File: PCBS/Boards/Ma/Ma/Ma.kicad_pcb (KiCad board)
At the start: 2 copper layers, 25 x 25 mm, 15 parts, among them J1 Conn_01x20_Socket, J2 Programmer, J3 PWM CHANNELS, J4 OLED SCREEN, SW1 SW_SPST, U1 ATmega328P-M, Y1 16MHz

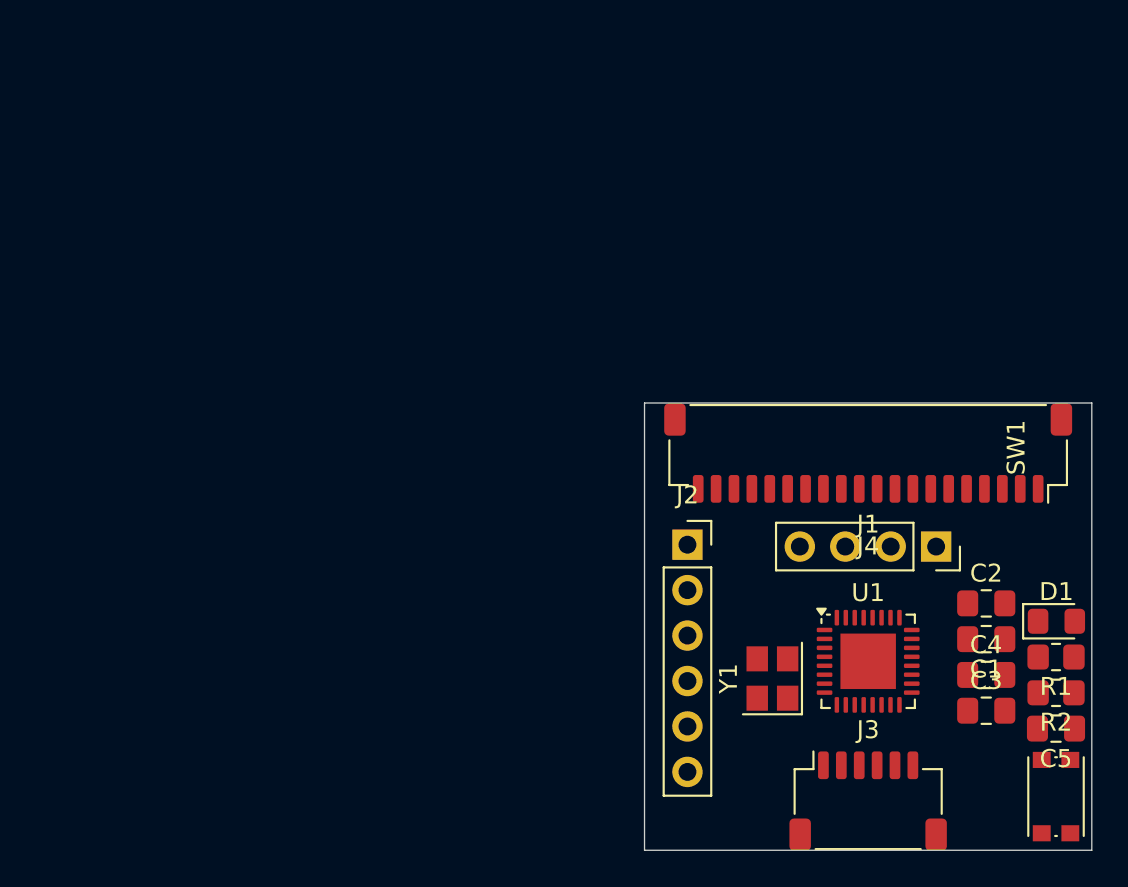
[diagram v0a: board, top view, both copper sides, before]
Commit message: creates schematic and PCB for MA minisumo board
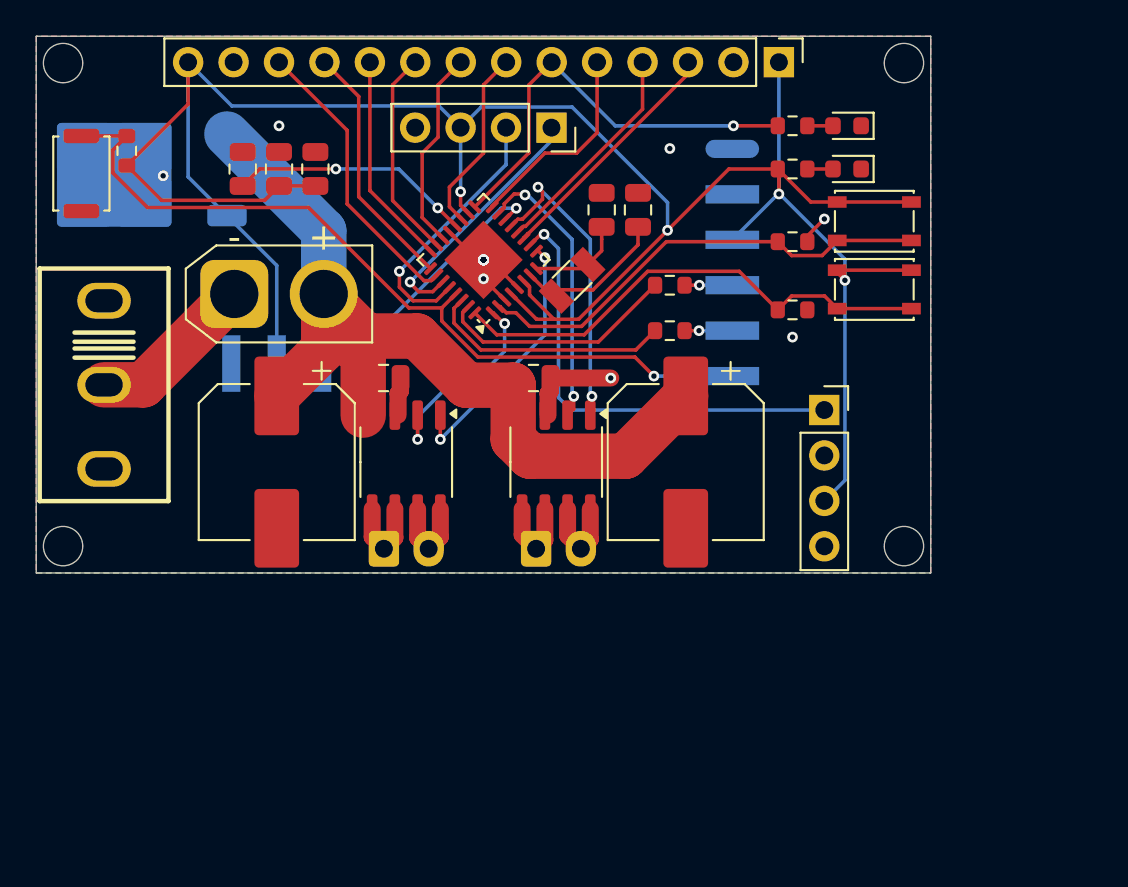
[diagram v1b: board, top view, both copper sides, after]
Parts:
- added C10: 0.1uF, Capacitor_SMD:C_0805_2012Metric, F.Cu at (151.3, 78.6)
- added C11: 470uF, Capacitor_SMD:CP_Elec_8x10.5, F.Cu at (159.8, 83.3)
- added C12: 470uF, Capacitor_SMD:CP_Elec_8x10.5, F.Cu at (136.9, 83.3)
- added C13: 0.1uF, Capacitor_SMD:C_0805_2012Metric, F.Cu at (142.9, 78.6)
- added D2: LED, LED_SMD:LED_0603_1608Metric, F.Cu at (168.8, 66.9)
- added H1: MountingHole, MountingHole:MountingHole_2.2mm_M2, F.Cu at (125.0, 61.0)
- added H2: MountingHole, MountingHole:MountingHole_2.2mm_M2, F.Cu at (172.0, 61.0)
- added H3: MountingHole, MountingHole:MountingHole_2.2mm_M2, F.Cu at (125.0, 88.0)
- added H4: MountingHole, MountingHole:MountingHole_2.2mm_M2, F.Cu at (172.0, 88.0)
- added J10: Conn_01x14_Pin, Connector_PinHeader_2.54mm:PinHeader_1x14_P2.54mm_Vertical, F.Cu at (165.0, 61.0)
- added J5: Conn_01x03_Pin, Package_TO_SOT_SMD:TO-252-2, B.Cu at (129.1, 67.2)
- added J7: Conn_01x03_Pin, EasyEDA:HDR-SMD_3P-P2.54-H-M-W13.3-N, B.Cu at (136.9, 77.8)
- added J8: Conn_01x06_Socket, EasyEDA:HDR-SMD_6P-P2.54-H-F-W11.7, B.Cu at (162.4, 72.1)
- added J9: Conn_01x04_Socket, Connector_PinSocket_2.54mm:PinSocket_1x04_P2.54mm_Vertical, F.Cu at (167.6, 80.4)
- added R3: R, Resistor_SMD:R_0603_1608Metric, F.Cu at (165.8, 64.5)
- added R4: R, Resistor_SMD:R_0603_1608Metric, F.Cu at (128.6, 65.9)
- added R5: R, Resistor_SMD:R_0603_1608Metric, F.Cu at (165.8, 71.0)
- added R6: R, Resistor_SMD:R_0603_1608Metric, F.Cu at (165.8, 74.8)
- added R7: R, Resistor_SMD:R_0603_1608Metric, F.Cu at (165.8, 66.9)
- added SW2: SW_SPDT, EasyEDA:SW-TH_XKB_SS-12M11XX, F.Cu at (127.3, 79.0)
- added SW3: SW_Push, Button_Switch_SMD:SW_SPST_PTS810, F.Cu at (170.3, 69.8)
- added SW4: SW_Push, Button_Switch_SMD:SW_SPST_PTS810, F.Cu at (170.3, 73.7)
- added U3: ~, Package_SO:SOP-8_3.9x4.9mm_P1.27mm, F.Cu at (152.6, 83.3)
- added U4: ~, Package_SO:SOP-8_3.9x4.9mm_P1.27mm, F.Cu at (144.2, 83.3)
- C1, C2, C3, C5: value C -> 0.1uF; footprint Capacitor_SMD:C_0805_2012Metric_Pad1.18x1.45mm_HandSolder -> Capacitor_SMD:C_0805_2012Metric
- C4: value C -> 4.7uF; footprint Capacitor_SMD:C_0805_2012Metric_Pad1.18x1.45mm_HandSolder -> Capacitor_SMD:C_0805_2012Metric
- D1: footprint LED_SMD:LED_0805_2012Metric_Pad1.15x1.40mm_HandSolder -> LED_SMD:LED_0603_1608Metric
- J1: value Conn_01x20_Socket -> Conn_01x02_Socket; footprint Connector_JST2:JST_SH_SM20B-SRSS-TB_1x20-1MP_P1.00mm_Horizontal -> Connector_AMASS:AMASS_XT30U-M_1x02_P5.0mm_Vertical
- J2: value Programmer -> Conn_01x04_Socket; footprint Connector_PinSocket_2.54mm:PinSocket_1x06_P2.54mm_Vertical -> Connector_PinSocket_2.54mm:PinSocket_1x04_P2.54mm_Vertical
- J3: value PWM CHANNELS -> Conn_01x02_Pin; footprint Connector_JST:JST_SH_SM06B-SRSS-TB_1x06-1MP_P1.00mm_Horizontal -> Connector_JST:JST_XH_B2B-XH-A_1x02_P2.50mm_Vertical; moved to B.Cu
- J4: value OLED SCREEN -> Conn_01x02_Pin; footprint Connector_PinSocket_2.54mm:PinSocket_1x04_P2.54mm_Vertical -> Connector_JST:JST_XH_B2B-XH-A_1x02_P2.50mm_Vertical; moved to B.Cu
- R1, R2: footprint Resistor_SMD:R_0805_2012Metric_Pad1.20x1.40mm_HandSolder -> Resistor_SMD:R_0603_1608Metric
- SW1: value SW_SPST -> SW_Push; footprint Button_Switch_SMD:SW_Push_1P1T_NO_CK_KMR2 -> Button_Switch_SMD:SW_Push_SPST_NO_Alps_SKRK
- Y1: value 16MHz -> Crystal; footprint Crystal:Crystal_SMD_3225-4Pin_3.2x2.5mm -> Crystal:Crystal_SMD_3215-2Pin_3.2x1.5mm
- moved SW1 64.7 mm to (126.0, 67.2), turned to -90 degrees
- moved C5 53.5 mm to (137.1, 66.9), turned to 90 degrees
- moved C1 49.2 mm to (135.0, 66.9), turned to -90 degrees
- moved C4 47.0 mm to (139.1, 66.9), turned to 90 degrees
- moved J1 36.5 mm to (134.6, 73.9), turned to 0 degrees
- moved C3 35.3 mm to (155.1, 69.2), turned to 90 degrees
- moved R2 31.4 mm to (158.9, 73.4), turned to 0 degrees
- moved U1 31.1 mm to (148.5, 72.0), turned to 135 degrees
- moved J4 30.9 mm to (142.9, 88.1), turned to 0 degrees
- moved D1 30.1 mm to (168.8, 64.5), turned to 180 degrees
- moved C2 29.4 mm to (157.1, 69.2), turned to 90 degrees
- moved R1 28.3 mm to (158.9, 76.0), turned to 0 degrees
- moved Y1 24.9 mm to (153.5, 73.1), turned to 45 degrees
- moved J2 24.5 mm to (152.3, 64.6), turned to -90 degrees
- moved J3 23.3 mm to (151.4, 88.1)
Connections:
- C2 pad 1: /RESET -> Net-(U1-XTAL1/PB6)
- C2 pad 2: DTR -> GND
- C3 pad 1: Net-(U1-XTAL1/PB6) -> Net-(U1-XTAL2/PB7)
- C4 pad 1: Net-(U1-XTAL2/PB7) -> +5V
- C5 pad 1: VCC -> +5V
- J1 pad 1: A7 -> Net-(J1-Pin_1)
- J1 pad 2: A6 -> +BATT
- J2 pad 1: DTR -> /SDA
- J2 pad 2: TXO -> /SCL
- J2 pad 3: RXI -> +5V
- J2 pad 4: VCC -> GND
- J3 pad 1: D10 -> Net-(J3-Pin_1)
- J3 pad 2: D9 -> Net-(J3-Pin_2)
- J4 pad 1: SDA -> Net-(J4-Pin_1)
- J4 pad 2: SCL -> Net-(J4-Pin_2)
- R1 pad 1: Net-(D1-A) -> Net-(U1-PD0)
- R1 pad 2: SCK -> /TX
- R2 pad 1: VCC -> Net-(U1-PD1)
- R2 pad 2: /RESET -> /RX
- SW1 pad 1: GND -> Reset
- SW1 pad 2: /RESET -> GND
- U1 pad 1: D3 -> /MA2
- U1 pad 10: D6 -> /START
- U1 pad 11: D7 -> /D7
- U1 pad 12: D8 -> /D8
- U1 pad 13: D9 -> /MB1
- U1 pad 14: D10 -> /SERVO
- U1 pad 15: MOSI -> /MB2
- U1 pad 16: MISO -> /D12
- U1 pad 17: SCK -> /D13
- U1 pad 18: VCC -> +5V
- U1 pad 19: unconnected-(U1-ADC6-Pad19) -> /A6
- U1 pad 2: D4 -> /BTN1
- U1 pad 22: unconnected-(U1-ADC7-Pad22) -> /A7
- U1 pad 23: A0 -> /A0
- U1 pad 24: A1 -> /A1
- U1 pad 25: A2 -> /A2
- U1 pad 26: A3 -> /A3
- U1 pad 27: SDA -> /SDA
- U1 pad 28: SCL -> /SCL
- U1 pad 29: /RESET -> Reset
- U1 pad 30: RXI -> Net-(U1-PD0)
- U1 pad 31: TXO -> Net-(U1-PD1)
- U1 pad 32: D2 -> /BTN2
- U1 pad 4: VCC -> +5V
- U1 pad 6: VCC -> +5V
- U1 pad 9: D5 -> /MA1
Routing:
- net +5V: track 0.00 -> 141.9 mm, vias 0 -> 4
- net +BATT: track 0.00 -> 52.8 mm
- net Reset: track 0.00 -> 45.8 mm, vias 0 -> 1
- net /BTN2: track 0.00 -> 27.9 mm
- net /BTN1: track 0.00 -> 26.2 mm
- net /START: track 0.00 -> 25.7 mm, vias 0 -> 1
- net /D13: track 0.00 -> 24.0 mm, vias 0 -> 1
- net /MB1: track 0.00 -> 17.2 mm, vias 0 -> 2
- net /A3: track 0.00 -> 16.4 mm
- net GND: track 0.00 -> 16.4 mm, vias 0 -> 18
- net /MB2: track 0.00 -> 15.7 mm, vias 0 -> 2
- net /SERVO: track 0.00 -> 15.3 mm, vias 0 -> 1
- net /SCL: track 0.00 -> 14.8 mm, vias 0 -> 1
- net /MA1: track 0.00 -> 14.6 mm, vias 0 -> 2
- net /SDA: track 0.00 -> 14.3 mm, vias 0 -> 1
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- added copper zone on B.Cu, net GND
- added copper zone on F.Cu, net GND
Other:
- board size 25 x 25 mm -> 50 x 30 mm

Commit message: updates MA PCB, adds logos
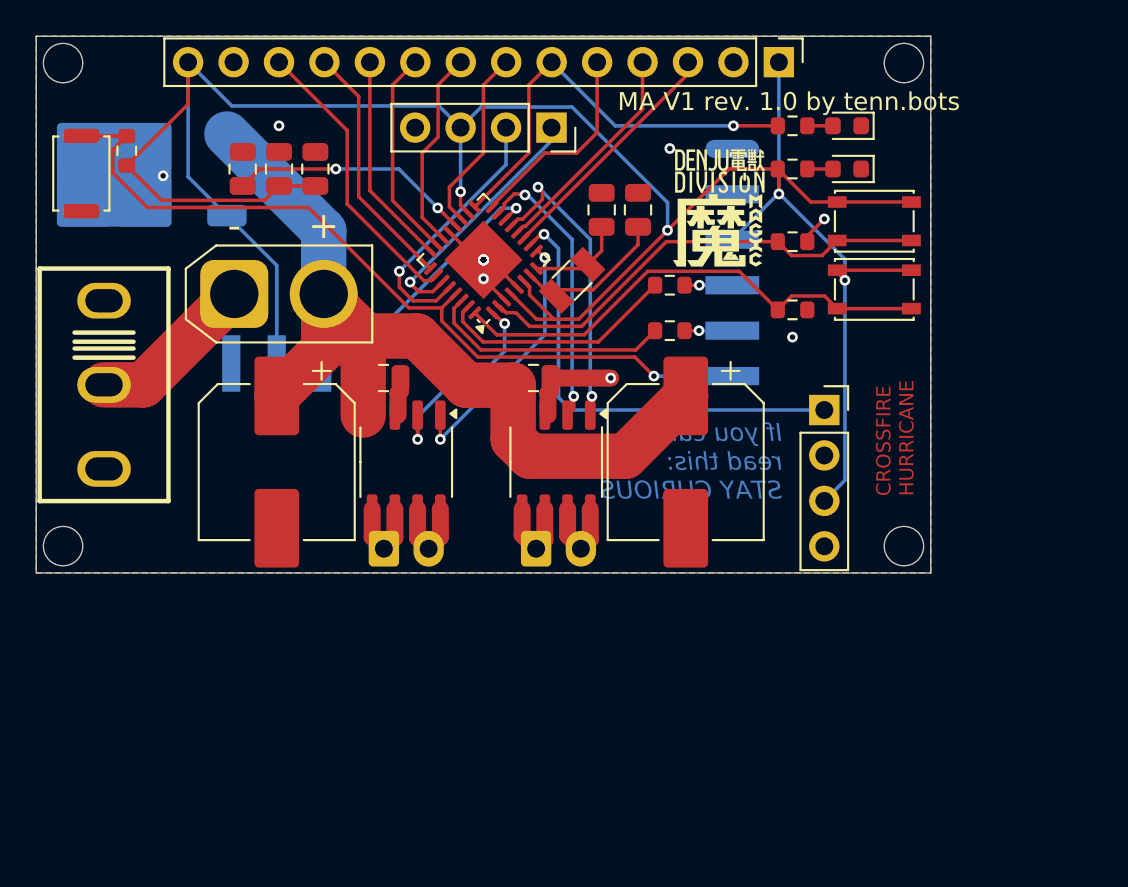
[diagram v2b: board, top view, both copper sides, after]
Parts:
- added G***: LOGO, LOGO, F.Cu at (161.7, 67.0)
- added G***: LOGO, LOGO, F.Cu at (161.6, 70.3)
- added G***: LOGO, LOGO, B.Cu at (148.8, 81.5)
- added G***: LOGO, LOGO, B.Cu at (148.9, 71.6)
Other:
- board text added: "CROSSFIRE HURRICANE"
- board text added: "If you can read this: STAY CURIOUS"
- board text added: "MA V1 rev. 1.0 by tenn.bots"
